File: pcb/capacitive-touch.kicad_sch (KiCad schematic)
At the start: 6 parts, among them J4 Conn_02x03_Odd_Even, U6 CAP1188

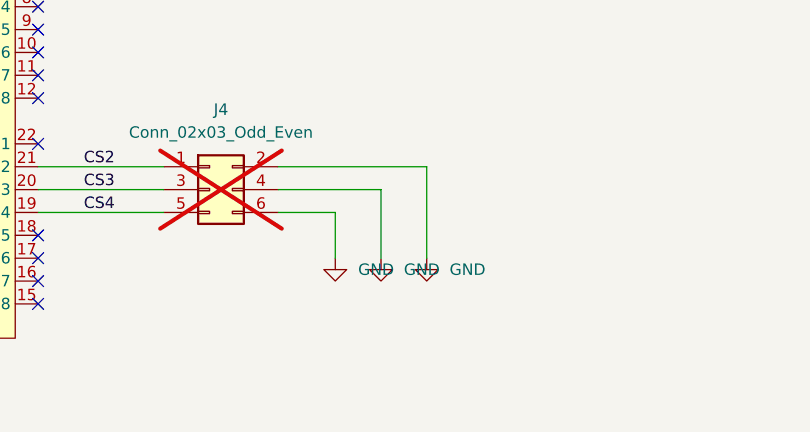
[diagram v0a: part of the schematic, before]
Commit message: Prepare schematic for revision 2.0.0
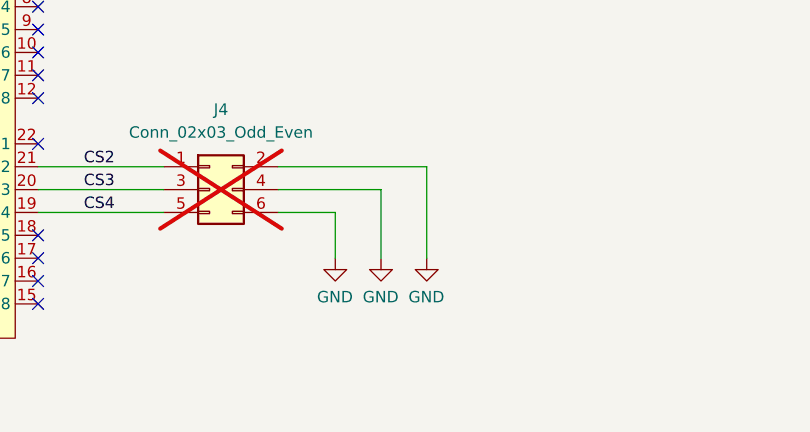
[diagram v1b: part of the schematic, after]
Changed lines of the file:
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@@
 		(title "Capacitive Touch")
 		(date "2025-04-27")
-		(rev "A")
+		(rev "2.0.0")
 		(company "George Sleen")
 	)
@@
 			)
 		)
-		(property "LCSC Part" ""
-			(at 121.92 95.25 0)
-			(effects
-				(font
-					(size 1.27 1.27)
-				)
-			)
-		)
 		(pin "20"
 		)
@@
 			)
 		)
-		(property "LCSC Part" ""
-			(at 107.95 58.42 0)
-			(effects
-				(font
-					(size 1.27 1.27)
-				)
-			)
-		)
 		(pin "2"
 		)
@@
 		(on_board yes)
 		(dnp no)
-		(fields_autoplaced yes)
 		(property "Reference" "#PWR074"
 			(at 186.69 116.84 0)
@@
 		)
 		(property "Value" "GND"
-			(at 189.23 111.7599 0)
+			(at 184.658 114.808 0)
 			(effects
 				(font
@@
 		(on_board yes)
 		(dnp no)
-		(fields_autoplaced yes)
 		(property "Reference" "#PWR072"
 			(at 176.53 116.84 0)
@@
 		)
 		(property "Value" "GND"
-			(at 179.07 111.7599 0)
+			(at 174.498 114.808 0)
 			(effects
 				(font
@@
 		(on_board yes)
 		(dnp no)
-		(fields_autoplaced yes)
 		(property "Reference" "#PWR073"
 			(at 181.61 116.84 0)
@@
 		)
 		(property "Value" "GND"
-			(at 184.15 111.7599 0)
+			(at 179.578 114.808 0)
 			(effects
 				(font
@@
 			)
 		)
-		(property "LCSC Part" ""
-			(at 72.39 88.9 0)
-			(effects
-				(font
-					(size 1.27 1.27)
-				)
-			)
-		)
 		(pin "2"
 		)
@@
 			)
 		)
-		(property "LCSC Part" ""
-			(at 83.82 88.9 0)
-			(effects
-				(font
-					(size 1.27 1.27)
-				)
-			)
-		)
 		(pin "2"
 		)
@@
 			)
 		)
-		(property "LCSC Part" ""
-			(at 162.56 102.87 0)
-			(effects
-				(font
-					(size 1.27 1.27)
-				)
-			)
-		)
 		(pin "5"
 		)
@@
 			)
 		)
-		(property "LCSC Part" ""
-			(at 72.39 67.31 0)
-			(effects
-				(font
-					(size 1.27 1.27)
-				)
-			)
-		)
